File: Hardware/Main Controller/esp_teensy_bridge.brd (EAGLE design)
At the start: 99.8 x 88.1 mm, 67 parts, among them IC1 BQ79600PWRQ1, Q5 VISHAY_SIS862DN-T1-GE3VISHAY_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, Q6 VISHAY_SIS862DN-T1-GE3VISHAY_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, Q7 VISHAY_SIS862DN-T1-GE3VISHAY_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, Q8 VISHAY_SIS862DN-T1-GE3VISHAY_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, U1 MCP2562-E/SN, U2 ESP32-DEVKITC-32D, X1 5566-12

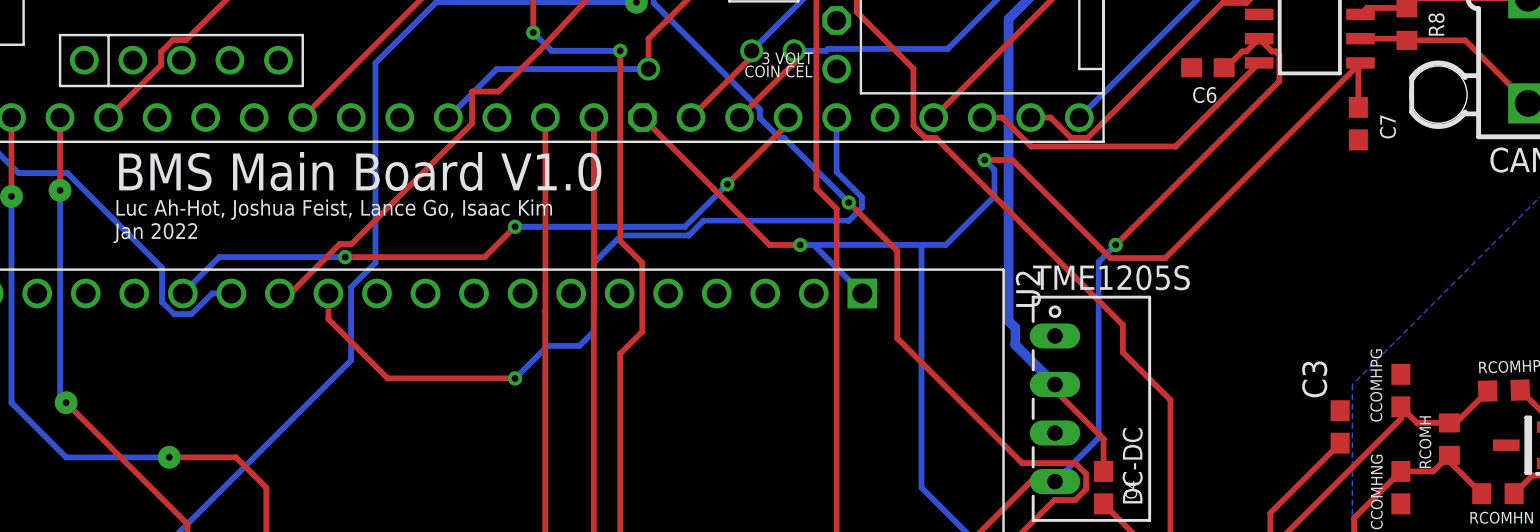
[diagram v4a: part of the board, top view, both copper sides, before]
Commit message: tactile switch
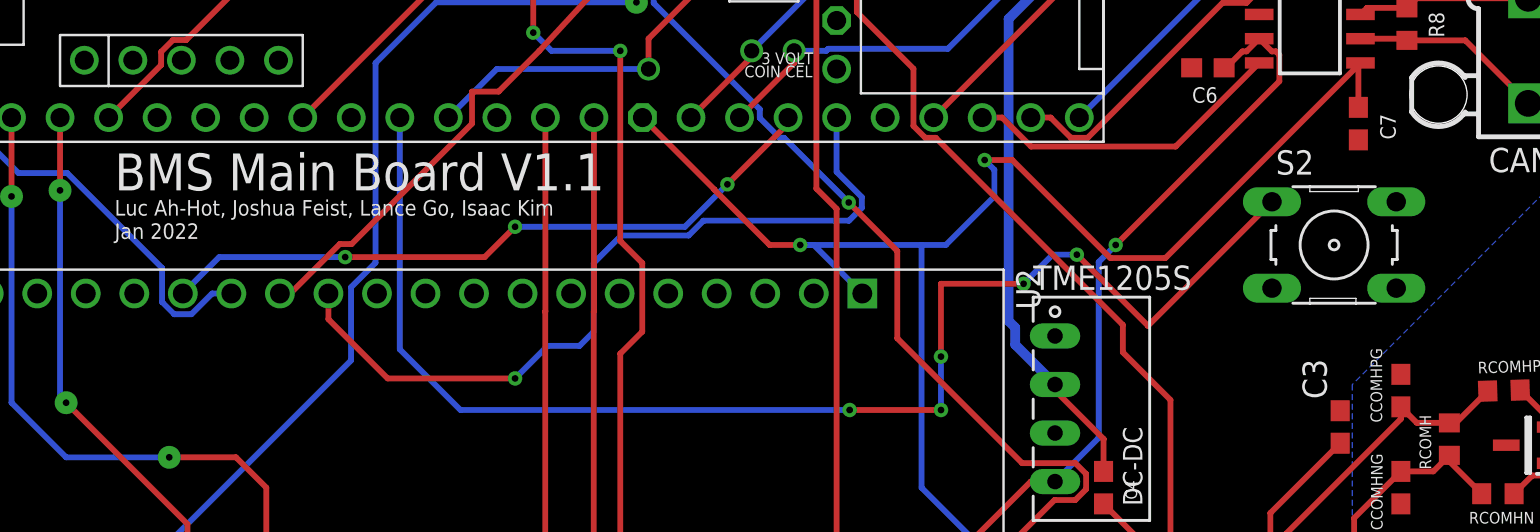
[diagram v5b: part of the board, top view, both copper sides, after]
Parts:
- added S2: (no value), switch-omron:B3F-10XX
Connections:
- new net N$7: S2.1, U$3.8-TX2/IN1
- net GND: now also S2.3
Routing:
- net N$7: track 0.00 -> 70.6 mm, vias 0 -> 5
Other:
- board text added: "BMS Main Board V1.1"
- board text removed: "BMS Main Board V1.0"
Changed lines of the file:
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@@
 <setting verticaltext="up"/>
 </settings>
-<grid distance="50" unitdist="mil" unit="mil" style="lines" multiple="1" display="yes" altdistance="5" altunitdist="mil" altunit="mil"/>
+<grid distance="10" unitdist="mil" unit="mil" style="lines" multiple="1" display="yes" altdistance="5" altunitdist="mil" altunit="mil"/>
 <layers>
 <layer number="1" name="Top" color="4" fill="1" visible="yes" active="yes"/>
@@
 <hole x="95.25" y="83.82" drill="4.445"/>
 <hole x="4.445" y="83.5025" drill="4.445"/>
-<text x="9.8425" y="43.4975" size="1.9304" layer="21">BMS Main Board V1.0</text>
+<text x="9.8425" y="43.4975" size="1.9304" layer="21">BMS Main Board V1.1</text>
 <text x="9.8425" y="40.9575" size="0.8128" layer="21">Luc Ah-Hot, Joshua Feist, Lance Go, Isaac Kim
 Jan 2022</text>
@@
 <attribute name="VALUE" x="0.2798" y="39.4146" size="1.27133125" layer="27" rot="R270"/>
 </element>
+<element name="S2" library="switch-omron" library_urn="urn:adsk.eagle:library:377" package="B3F-10XX" package3d_urn="urn:adsk.eagle:package:27496/1" value="" x="73.66" y="40.64" smashed="yes">
+<attribute name="MF" value="" x="73.66" y="40.64" size="1.778" layer="27" display="off"/>
+<attribute name="MPN" value="B3F-1000" x="73.66" y="40.64" size="1.778" layer="27" display="off"/>
+<attribute name="NAME" x="70.612" y="44.323" size="1.27" layer="25" ratio="10"/>
+<attribute name="OC_FARNELL" value="176432" x="73.66" y="40.64" size="1.778" layer="27" display="off"/>
+<attribute name="OC_NEWARK" value="36M3542" x="73.66" y="40.64" size="1.778" layer="27" display="off"/>
+<attribute name="POPULARITY" value="72" x="73.66" y="40.64" size="1.778" layer="27" display="off"/>
+<attribute name="VALUE" x="70.612" y="35.56" size="1.27" layer="27" ratio="10"/>
+</element>
 </elements>
 <signals>
@@
 <wire x1="48.5775" y1="55.88" x2="49.53" y2="55.88" width="0.3048" layer="16"/>
 <via x="49.53" y="55.88" extent="1-16" drill="0.35"/>
+<contactref element="S2" pad="3"/>
 </signal>
 <signal name="N$1">
@@
 <contactref element="U2" pad="20"/>
 </signal>
+<signal name="N$7">
+<contactref element="S2" pad="1"/>
+<contactref element="U$3" pad="8-TX2/IN1"/>
+<wire x1="63.92" y1="36.41" x2="60.198" y2="40.132" width="0.3048" layer="1"/>
+<via x="60.198" y="40.132" extent="1-16" drill="0.35"/>
+<wire x1="60.198" y1="40.132" x2="58.928" y2="40.132" width="0.3048" layer="16"/>
+<wire x1="58.928" y1="40.132" x2="57.404" y2="38.608" width="0.3048" layer="16"/>
+<wire x1="57.404" y1="38.608" x2="57.4092" y2="38.608" width="0.3048" layer="16"/>
+<via x="57.4092" y="38.608" extent="1-16" drill="0.35"/>
+<wire x1="57.4092" y1="38.608" x2="53.086" y2="38.608" width="0.3048" layer="1"/>
+<wire x1="53.086" y1="38.608" x2="53.086" y2="34.798" width="0.3048" layer="1"/>
+<via x="53.086" y="34.798" extent="1-16" drill="0.35"/>
+<wire x1="53.086" y1="34.798" x2="53.086" y2="32.004" width="0.3048" layer="16"/>
+<via x="53.086" y="32.004" extent="1-16" drill="0.35"/>
+<wire x1="53.086" y1="32.004" x2="48.308" y2="32.004" width="0.3048" layer="1"/>
+<wire x1="48.308" y1="32.004" x2="48.26" y2="32.004" width="0.3048" layer="1"/>
+<via x="48.308" y="32.004" extent="1-16" drill="0.35"/>
+<wire x1="48.308" y1="32.004" x2="27.94" y2="32.004" width="0.3048" layer="16"/>
+<wire x1="24.765" y1="35.179" x2="24.765" y2="47.3075" width="0.3048" layer="16"/>
+<wire x1="27.94" y1="32.004" x2="24.765" y2="35.179" width="0.3048" layer="16"/>
+<wire x1="63.92" y1="36.4118" x2="63.92" y2="36.41" width="0.3048" layer="1"/>
+<wire x1="70.4088" y1="42.9006" x2="63.92" y2="36.4118" width="0.3048" layer="1"/>
+</signal>
 </signals>
